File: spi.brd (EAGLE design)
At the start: 35.2 x 33 mm, 5 parts, among them IC2 25AA080SN, IC3 25AA080P, X1 2510-

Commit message: Добавлены конденсаторы по питанию
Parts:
- added C1: 100n, resistor:C0805K
- added C2: 10 uF, resistor:SMC_D
- R1, R2: value (none) -> 330 Om
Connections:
- net GND: now also C1.2, C2.-
- net VCC: now also C1.1, C2.+
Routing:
- net VCC: track 84.8 -> 90.8 mm
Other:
- board size 35.2 x 33 mm -> 40.3 x 33 mm
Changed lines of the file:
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@@
 <?xml version="1.0" encoding="utf-8"?>
 <!DOCTYPE eagle SYSTEM "eagle.dtd">
-<eagle version="9.1.1">
+<eagle version="9.5.2">
 <drawing>
 <settings>
@@
 <board>
 <plain>
-<wire x1="8.89" y1="16.51" x2="44.12" y2="16.51" width="0" layer="20"/>
+<wire x1="3.81" y1="16.51" x2="44.12" y2="16.51" width="0" layer="20"/>
 <wire x1="44.12" y1="16.51" x2="44.12" y2="49.52" width="0" layer="20"/>
-<wire x1="44.12" y1="49.52" x2="8.89" y2="49.52" width="0" layer="20"/>
-<wire x1="8.89" y1="49.52" x2="8.89" y2="16.51" width="0" layer="20"/>
+<wire x1="44.12" y1="49.52" x2="3.81" y2="49.52" width="0" layer="20"/>
+<wire x1="3.81" y1="49.52" x2="3.81" y2="16.51" width="0" layer="20"/>
 <polygon width="0.3048" layer="42">
 <vertex x="20" y="27.94"/>
@@
 </autorouter>
 <elements>
-<element name="IC2" library="microchip" library_urn="urn:adsk.eagle:library:294" package="SO-08" package3d_urn="urn:adsk.eagle:package:20804/2" value="25AA080SN" x="19.05" y="29.21" rot="MR270">
+<element name="IC2" library="microchip" library_urn="urn:adsk.eagle:library:294" package="SO-08" package3d_urn="urn:adsk.eagle:package:20804/2" value="25AA080SN" x="19.05" y="29.21" smashed="yes" rot="MR270">
 <attribute name="MF" value="MICROCHIP" x="19.05" y="29.21" size="1.778" layer="28" rot="MR270" display="off"/>
 <attribute name="MPN" value="25AA080/SN" x="19.05" y="29.21" size="1.778" layer="28" rot="MR270" display="off"/>
+<attribute name="NAME" x="20.955" y="31.877" size="1.27" layer="26" rot="MR0"/>
 <attribute name="OC_FARNELL" value="1816072" x="19.05" y="29.21" size="1.778" layer="28" rot="MR270" display="off"/>
 <attribute name="OC_NEWARK" value="92C7351" x="19.05" y="29.21" size="1.778" layer="28" rot="MR270" display="off"/>
-</element>
-<element name="IC3" library="microchip" library_urn="urn:adsk.eagle:library:294" package="DIL8" package3d_urn="urn:adsk.eagle:package:20796/2" value="25AA080P" x="31.75" y="29.21" rot="R270">
+<attribute name="VALUE" x="20.955" y="25.273" size="1.27" layer="28" rot="MR0"/>
+</element>
+<element name="IC3" library="microchip" library_urn="urn:adsk.eagle:library:294" package="DIL8" package3d_urn="urn:adsk.eagle:package:20796/2" value="25AA080P" x="31.75" y="29.21" smashed="yes" rot="R270">
 <attribute name="MF" value="MICROCHIP" x="31.75" y="29.21" size="1.778" layer="27" rot="R270" display="off"/>
 <attribute name="MPN" value="25AA080/P" x="31.75" y="29.21" size="1.778" layer="27" rot="R270" display="off"/>
+<attribute name="NAME" x="29.21" y="34.4678" size="1.778" layer="25" ratio="10"/>
 <attribute name="OC_FARNELL" value="1331352" x="31.75" y="29.21" size="1.778" layer="27" rot="R270" display="off"/>
 <attribute name="OC_NEWARK" value="92C7349" x="31.75" y="29.21" size="1.778" layer="27" rot="R270" display="off"/>
-</element>
-<element name="X1" library="con-3m" library_urn="urn:adsk.eagle:library:119" package="PAK100/2500-10" package3d_urn="urn:adsk.eagle:package:5571/1" value="2510-" x="25.4" y="44.45">
+<attribute name="VALUE" x="29.21" y="21.971" size="1.778" layer="27" ratio="10"/>
+</element>
+<element name="X1" library="con-3m" library_urn="urn:adsk.eagle:library:119" package="PAK100/2500-10" package3d_urn="urn:adsk.eagle:package:5571/1" value="2510-" x="25.4" y="44.45" smashed="yes">
 <attribute name="MF" value="3M" x="25.4" y="44.45" size="1.778" layer="27" display="off"/>
 <attribute name="MPN" value="2510-6002UB" x="25.4" y="44.45" size="1.778" layer="27" display="off"/>
+<attribute name="NAME" x="15.24" y="49.022" size="1.27" layer="25"/>
 <attribute name="OC_FARNELL" value="9838244" x="25.4" y="44.45" size="1.778" layer="27" display="off"/>
 <attribute name="OC_NEWARK" value="46F4725" x="25.4" y="44.45" size="1.778" layer="27" display="off"/>
-</element>
-<element name="R1" library="eagle-ltspice" library_urn="urn:adsk.eagle:library:217" package="0204/7" package3d_urn="urn:adsk.eagle:package:13274/1" value="" x="24.13" y="31.75" rot="R270">
+<attribute name="VALUE" x="22.86" y="49.022" size="1.27" layer="27"/>
+</element>
+<element name="R1" library="eagle-ltspice" library_urn="urn:adsk.eagle:library:217" package="0204/7" package3d_urn="urn:adsk.eagle:package:13274/1" value="330 Om" x="24.13" y="31.75" smashed="yes" rot="R270">
+<attribute name="NAME" x="21.6154" y="29.21" size="0.9906" layer="25" ratio="10" rot="R270"/>
 <attribute name="SPICEMODEL" value="NONE" x="24.13" y="31.75" size="1.778" layer="27" rot="R270" display="off"/>
 <attribute name="SPICEPREFIX" value="R" x="24.13" y="31.75" size="1.778" layer="27" rot="R270" display="off"/>
-</element>
-<element name="R2" library="eagle-ltspice" library_urn="urn:adsk.eagle:library:217" package="0204/7" package3d_urn="urn:adsk.eagle:package:13274/1" value="" x="39.37" y="34.29" rot="R90">
+<attribute name="VALUE" x="21.1074" y="34.6456" size="0.9906" layer="27" ratio="10" rot="R270"/>
+</element>
+<element name="R2" library="eagle-ltspice" library_urn="urn:adsk.eagle:library:217" package="0204/7" package3d_urn="urn:adsk.eagle:package:13274/1" value="330 Om" x="39.37" y="34.29" smashed="yes" rot="R90">
+<attribute name="NAME" x="38.0746" y="31.75" size="0.9906" layer="25" ratio="10" rot="R90"/>
 <attribute name="SPICEMODEL" value="NONE" x="39.37" y="34.29" size="1.778" layer="27" rot="R90" display="off"/>
 <attribute name="SPICEPREFIX" value="R" x="39.37" y="34.29" size="1.778" layer="27" rot="R90" display="off"/>
+<attribute name="VALUE" x="39.8526" y="32.6644" size="0.9906" layer="27" ratio="10" rot="R90"/>
+</element>
+<element name="C1" library="resistor" library_urn="urn:adsk.eagle:library:348" package="C0805K" package3d_urn="urn:adsk.eagle:package:23681/2" value="100n" x="13.97" y="38.1" smashed="yes" rot="MR0">
+<attribute name="NAME" x="11.16" y="37.705" size="1.016" layer="26" rot="MR0"/>
+<attribute name="VALUE" x="12.43" y="36.2" size="1.016" layer="28" rot="MR0"/>
+</element>
+<element name="C2" library="resistor" library_urn="urn:adsk.eagle:library:348" package="SMC_D" package3d_urn="urn:adsk.eagle:package:25923/2" value="10 uF" x="11.43" y="41.91" smashed="yes" rot="MR0">
+<attribute name="NAME" x="15.08" y="44.21" size="1.27" layer="26" rot="MR0"/>
+<attribute name="VALUE" x="15.08" y="38.335" size="1.27" layer="28" rot="MR0"/>
 </element>
 </elements>
@@
 <wire x1="24.13" y1="35.56" x2="19.05" y2="35.56" width="0.8128" layer="16"/>
 <wire x1="19.05" y1="35.56" x2="17.78" y2="36.83" width="1.016" layer="16" curve="-90"/>
-<wire x1="17.78" y1="36.83" x2="17.78" y2="43.18" width="1.016" layer="16"/>
+<wire x1="17.78" y1="36.83" x2="17.78" y2="38.1" width="1.016" layer="16"/>
+<wire x1="17.78" y1="38.1" x2="17.78" y2="41.91" width="1.016" layer="16"/>
+<wire x1="17.78" y1="43.18" x2="17.78" y2="41.91" width="1.016" layer="16"/>
 <wire x1="17.78" y1="43.18" x2="20.32" y2="45.72" width="1.016" layer="16" curve="-90"/>
 <wire x1="36.83" y1="33.02" x2="38.1" y2="34.29" width="1.016" layer="16"/>
-<wire x1="16.51" y1="33.02" x2="16.51" y2="33.02" width="0.508" layer="16"/>
 <wire x1="16.51" y1="33.02" x2="17.78" y2="34.29" width="0.8128" layer="16"/>
 <wire x1="17.78" y1="34.29" x2="17.78" y2="36.83" width="0.8128" layer="16" curve="90"/>
+<contactref element="C2" pad="+"/>
+<contactref element="C1" pad="1"/>
+<wire x1="17.78" y1="41.91" x2="14.58" y2="41.91" width="1.016" layer="16"/>
+<wire x1="17.78" y1="38.1" x2="14.97" y2="38.1" width="1.016" layer="16"/>
 </signal>
 <signal name="SO">
@@
 <wire x1="27.94" y1="45.72" x2="30.48" y2="45.72" width="1.016" layer="16"/>
 <polygon width="0.3048" layer="16" isolate="0.5">
-<vertex x="8.89" y="49.53"/>
-<vertex x="8.89" y="16.51"/>
+<vertex x="3.81" y="49.53"/>
+<vertex x="3.81" y="36.83"/>
+<vertex x="17.78" y="36.83"/>
+<vertex x="17.78" y="16.51"/>
 <vertex x="43.18" y="16.51"/>
 <vertex x="43.18" y="43.18"/>
@@
 <vertex x="33.02" y="49.53"/>
 </polygon>
+<contactref element="C2" pad="-"/>
+<contactref element="C1" pad="2"/>
 </signal>
 </signals>
@@
 <mfgpreviewcolor name="substratecolor" color="0xFF786E46"/>
 </mfgpreviewcolors>
+<errors>
+</errors>
 </board>
 </drawing>

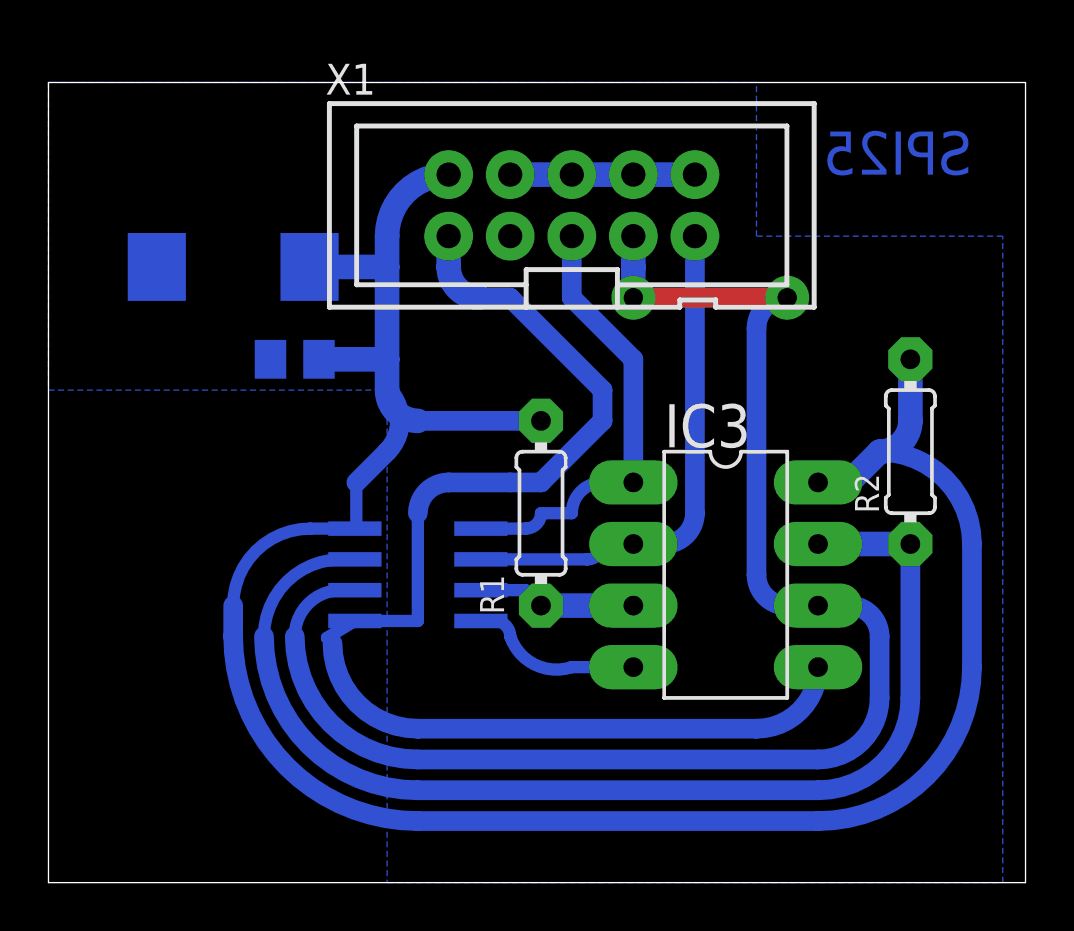
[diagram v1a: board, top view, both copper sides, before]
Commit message: Исправлено посадочное место под планарную микросхему
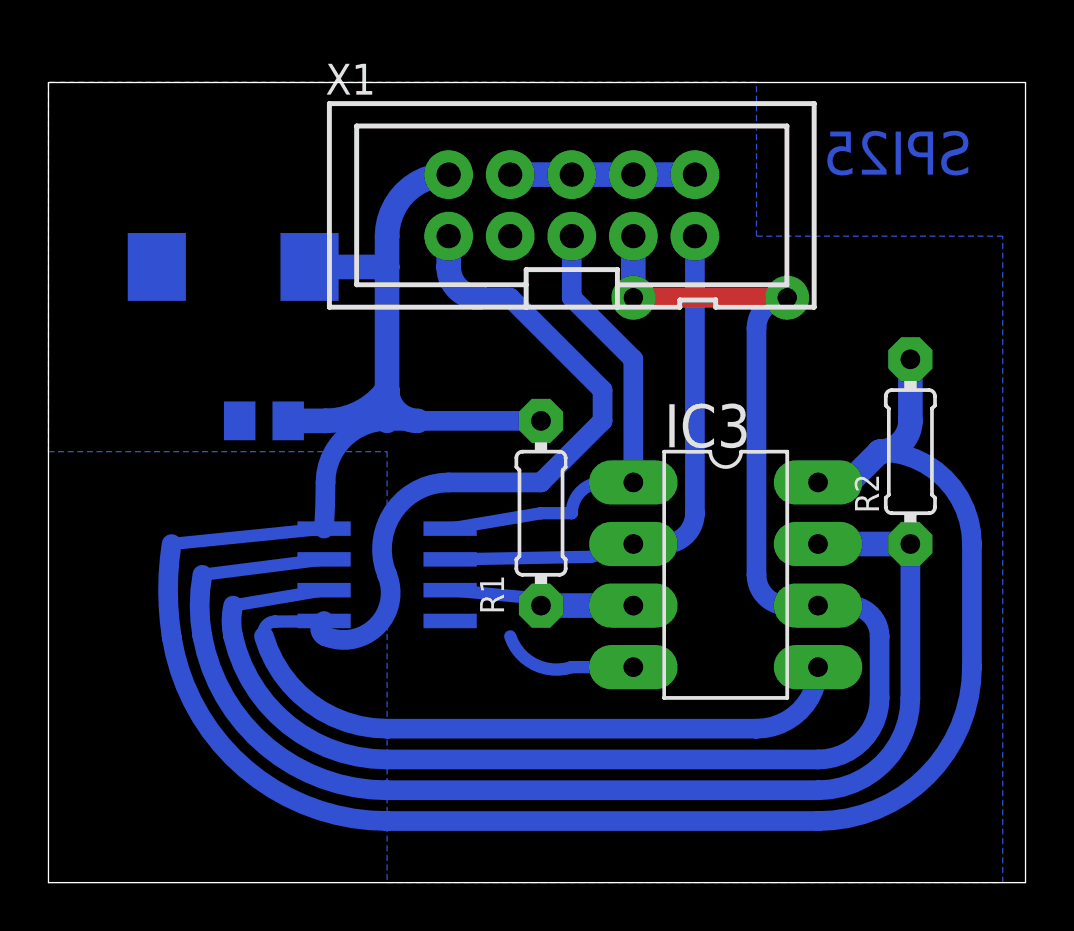
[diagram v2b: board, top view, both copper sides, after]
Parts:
- moved C1 2.84 mm to (12.7, 35.6)
- moved IC2 1.27 mm to (17.8, 29.2)
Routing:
- net VCC: track 90.8 -> 100.7 mm
- net HOLD: track 46.1 -> 50.8 mm
- net SCK: track 60.1 -> 64.1 mm
- net SI: track 51.4 -> 55.2 mm
- net GND: track 14.5 -> 13.0 mm
- net SO: track 21.0 -> 22.3 mm
- net WP: track 6.55 -> 7.70 mm
- net CS: track 18.3 -> 19.4 mm

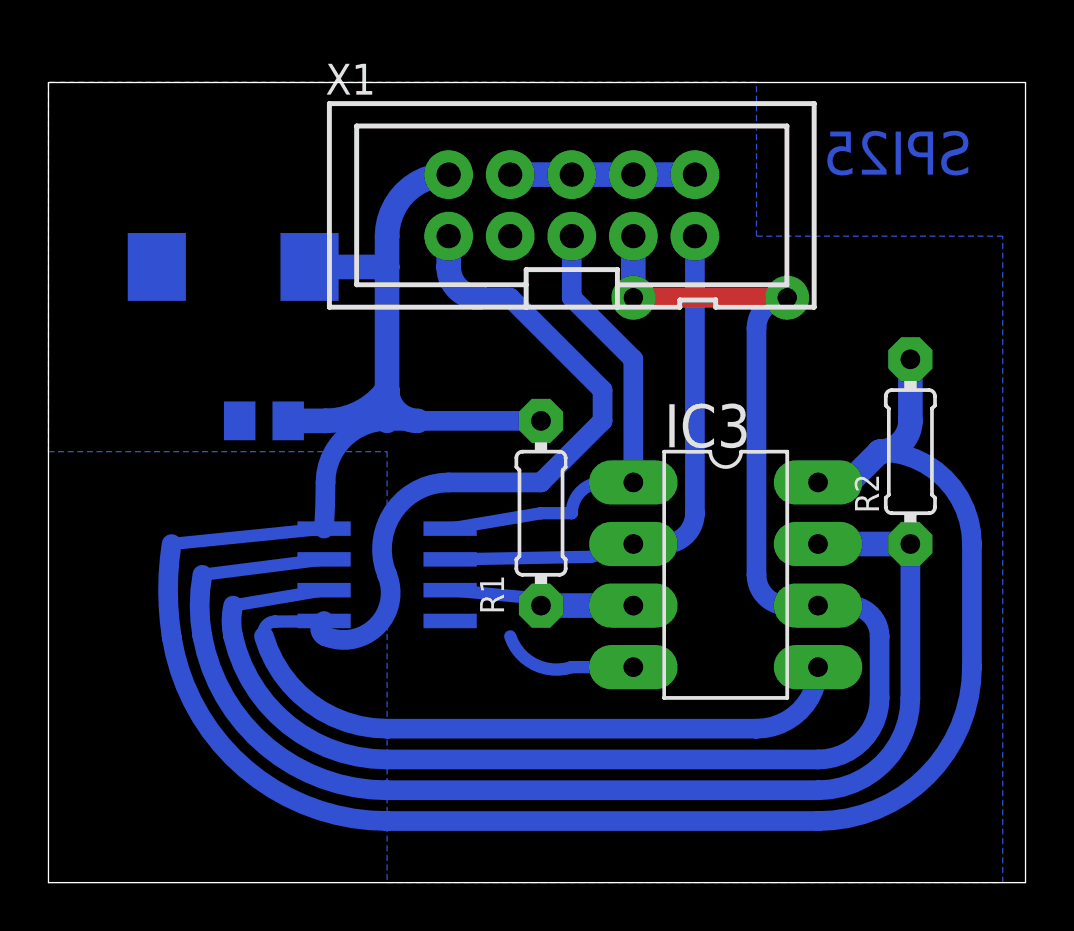
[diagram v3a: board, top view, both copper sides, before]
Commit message: Диаметр отверстий 0.3 мм, диаметр площадок 2.2 мм
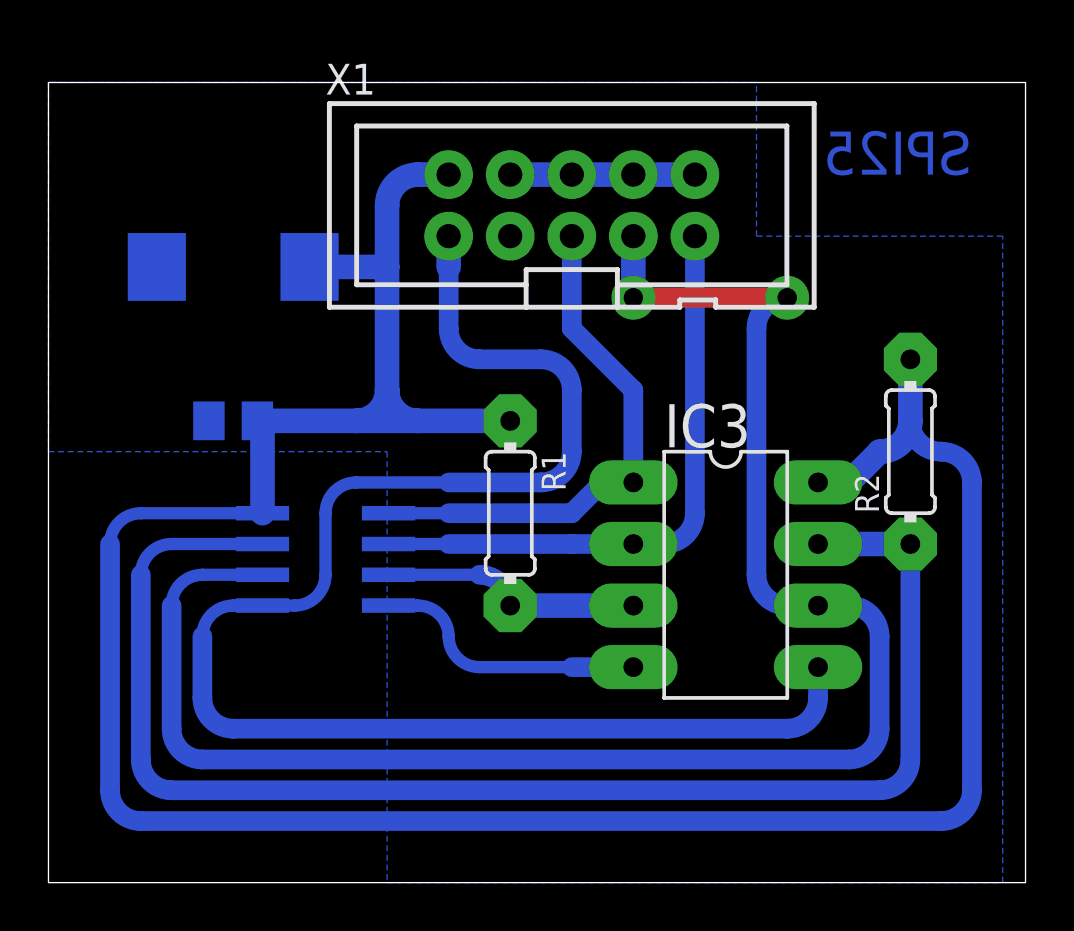
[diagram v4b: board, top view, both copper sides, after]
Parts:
- moved IC2 2.62 mm to (15.2, 29.8)
- moved C1 1.27 mm to (11.4, 35.6)
- moved R1 1.27 mm to (22.9, 31.8)
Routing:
- net VCC: track 100.7 -> 109.1 mm
- net HOLD: track 50.8 -> 58.7 mm
- net SI: track 55.2 -> 62.6 mm
- net SCK: track 64.1 -> 70.4 mm
- net GND: track 13.0 -> 18.8 mm
- net SO: track 22.3 -> 25.9 mm
- net WP: track 7.70 -> 11.3 mm
- net CS: track 19.4 -> 21.8 mm
